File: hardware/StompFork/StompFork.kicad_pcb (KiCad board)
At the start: 2 copper layers, 100.3 x 50.8 mm, 34 parts, among them J1 Line-Level Input, J2 Direct Output, J3 Stompbox Output 1, J4 Stompbox Output 2, J5 Power, U1 TL074

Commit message: Update PCB
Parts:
- moved D1 11.4 mm to (127.0, 116.8), turned to 180 degrees
- moved J1 9.14 mm to (185.4, 88.9)
- moved J3 8.03 mm to (185.4, 109.2)
- moved J4 8.03 mm to (185.4, 99.0)
- moved R13 8.03 mm to (127.0, 114.3), turned to 180 degrees
- moved J2 7.62 mm to (185.4, 119.3)
- moved C5 7.13 mm to (175.3, 121.8), turned to 90 degrees
- moved R5 5.68 mm to (157.5, 121.9)
- moved R8 5.68 mm to (157.5, 116.8)
- moved C6 5.08 mm to (175.3, 109.1)
- moved C7 5.08 mm to (175.3, 91.5)
- moved RV2 2.62 mm to (109.2, 84.0)
- moved RV1 2.62 mm to (109.2, 96.6)
- moved R10 2.54 mm to (157.5, 101.6)
- moved R6 2.54 mm to (157.5, 111.8)
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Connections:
- J1 pad 1: Net-(J1-T) -> GND
- J1 pad 2: GND -> Net-(J1-T)
- J2 pad 1: Net-(J2-T) -> GND
- J2 pad 2: GND -> Net-(J2-T)
- J3 pad 1: Net-(J3-T) -> GND
- J3 pad 2: GND -> Net-(J3-T)
- J4 pad 1: Net-(J4-T) -> GND
- J4 pad 2: GND -> Net-(J4-T)
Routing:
- net GND: track 266.9 -> 239.0 mm
- net Net-(D2-A): track 15.9 -> 8.67 mm
- net Net-(J1-T): track 33.4 -> 26.8 mm
- net Net-(J2-T): track 24.0 -> 17.8 mm
- net Net-(J3-T): track 24.9 -> 19.9 mm
- net Net-(J4-T): track 25.0 -> 19.9 mm
- net Net-(R2-Pad1): track 96.4 -> 93.7 mm
- net Net-(U1C-+): track 55.1 -> 57.7 mm
- net Net-(R4-Pad1): track 10.2 -> 7.62 mm
- net Net-(R3-Pad1): track 10.2 -> 7.62 mm
- net Net-(C6-Pad1): track 11.2 -> 8.75 mm
- net Net-(C5-Pad1): track 10.2 -> 7.77 mm
- net Net-(C7-Pad1): track 12.3 -> 11.2 mm
- net Net-(U1D-+): track 52.5 -> 51.4 mm
- net VCC: track 35.1 -> 34.1 mm

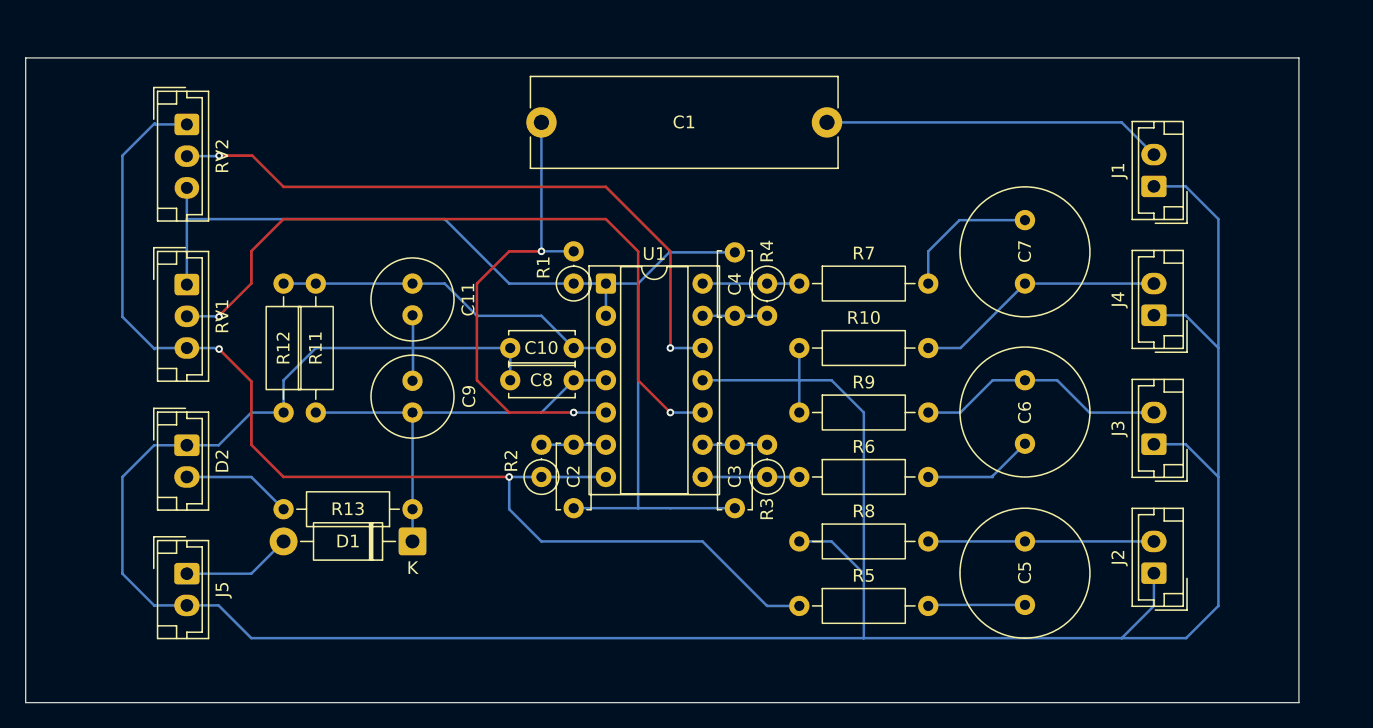
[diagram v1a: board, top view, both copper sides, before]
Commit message: Fix cap footprints
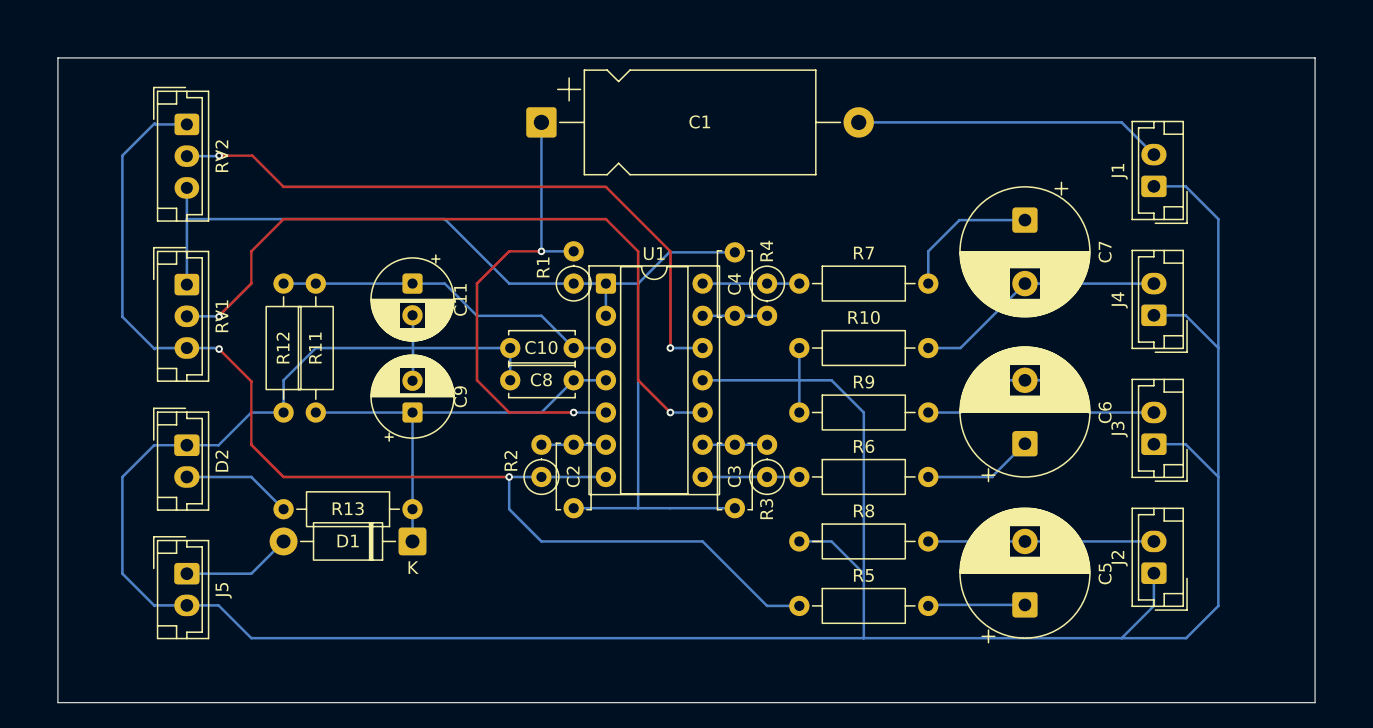
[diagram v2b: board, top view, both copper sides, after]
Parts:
- C1: footprint Capacitor_THT:C_Rect_L24.0mm_W7.0mm_P22.50mm_MKT -> Capacitor_THT:CP_Axial_L18.0mm_D8.0mm_P25.00mm_Horizontal
- C11, C9: footprint Capacitor_THT:C_Radial_D6.3mm_H11.0mm_P2.50mm -> Capacitor_THT:CP_Radial_D6.3mm_P2.50mm
- C5, C6, C7: footprint Capacitor_THT:C_Radial_D10.0mm_H12.5mm_P5.00mm -> Capacitor_THT:CP_Radial_D10.0mm_P5.00mm
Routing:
- net Net-(J1-T): track 26.8 -> 24.3 mm
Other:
- board size 100.3 x 50.8 mm -> 99.1 x 50.8 mm

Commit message: Update PCB
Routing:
- net GND: track 239.0 -> 231.4 mm
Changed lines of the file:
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@@
 	)
 	(segment
-		(start 116.84 116.84)
-		(end 114.3 119.38)
+		(start 114.3 116.84)
+		(end 116.84 116.84)
 		(width 0.2)
 		(layer "B.Cu")
@@
 	)
 	(segment
-		(start 114.3 119.38)
-		(end 109.22 119.38)
+		(start 111.76 119.38)
+		(end 114.3 116.84)
 		(width 0.2)
 		(layer "B.Cu")
 		(net 2)
+	)
+	(segment
+		(start 109.22 119.38)
+		(end 111.76 119.38)
+		(width 0.2)
+		(layer "B.Cu")
+		(net 2)
+	)
+	(segment
+		(start 147.32 114.22)
+		(end 152.4 114.22)
+		(width 0.2)
+		(layer "B.Cu")
+		(net 3)
+	)
+	(segment
+		(start 134.62 96.52)
+		(end 129.54 91.44)
+		(width 0.2)
+		(layer "B.Cu")
+		(net 3)
+	)
+	(segment
+		(start 139.7 114.22)
+		(end 144.78 114.22)
+		(width 0.2)
+		(layer "B.Cu")
+		(net 3)
+	)
+	(segment
+		(start 147.24 94.06)
+		(end 144.78 96.52)
+		(width 0.2)
+		(layer "B.Cu")
+		(net 3)
 	)
 	(segment
 		(start 129.54 91.44)
 		(end 109.22 91.44)
-		(width 0.2)
-		(layer "B.Cu")
-		(net 3)
-	)
-	(segment
-		(start 147.32 114.22)
-		(end 152.4 114.22)
-		(width 0.2)
-		(layer "B.Cu")
-		(net 3)
-	)
-	(segment
-		(start 134.62 96.52)
-		(end 129.54 91.44)
-		(width 0.2)
-		(layer "B.Cu")
-		(net 3)
-	)
-	(segment
-		(start 139.7 114.22)
-		(end 144.78 114.22)
-		(width 0.2)
-		(layer "B.Cu")
-		(net 3)
-	)
-	(segment
-		(start 147.24 94.06)
-		(end 144.78 96.52)
 		(width 0.2)
 		(layer "B.Cu")
@@
 	)
 	(segment
-		(start 111.72 109.26)
-		(end 109.22 109.26)
-		(width 0.2)
-		(layer "B.Cu")
-		(net 5)
-	)
-	(segment
 		(start 185.42 88.86)
 		(end 187.92 88.86)
@@
 	)
 	(segment
+		(start 190.5 116.84)
+		(end 190.5 111.76)
+		(width 0.2)
+		(layer "B.Cu")
+		(net 5)
+	)
+	(segment
 		(start 162.56 119.38)
 		(end 162.56 124.46)
@@
 	)
 	(segment
-		(start 114.3 106.68)
-		(end 111.72 109.26)
-		(width 0.2)
-		(layer "B.Cu")
-		(net 5)
-	)
-	(segment
-		(start 162.56 124.46)
-		(end 114.3 124.46)
-		(width 0.2)
-		(layer "B.Cu")
-		(net 5)
-	)
-	(segment
-		(start 190.5 111.76)
-		(end 190.5 121.92)
-		(width 0.2)
-		(layer "B.Cu")
-		(net 5)
-	)
-	(segment
 		(start 160.02 104.14)
 		(end 162.56 106.68)
@@
 	)
 	(segment
-		(start 190.5 121.92)
-		(end 187.96 124.46)
+		(start 149.86 121.92)
+		(end 152.4 124.46)
 		(width 0.2)
 		(layer "B.Cu")
@@
 	)
 	(segment
-		(start 114.3 124.46)
-		(end 111.72 121.88)
-		(width 0.2)
-		(layer "B.Cu")
-		(net 5)
-	)
-	(segment
-		(start 116.84 106.68)
-		(end 114.3 106.68)
+		(start 185.42 119.34)
+		(end 187.92 119.34)
+		(width 0.2)
+		(layer "B.Cu")
+		(net 5)
+	)
+	(segment
+		(start 152.4 124.46)
+		(end 162.56 124.46)
 		(width 0.2)
 		(layer "B.Cu")
@@
 	)
 	(segment
+		(start 111.76 121.92)
+		(end 149.86 121.92)
+		(width 0.2)
+		(layer "B.Cu")
+		(net 5)
+	)
+	(segment
 		(start 104.14 119.38)
 		(end 104.14 111.76)
@@
 	)
 	(segment
-		(start 111.72 121.88)
-		(end 109.22 121.88)
-		(width 0.2)
-		(layer "B.Cu")
-		(net 5)
-	)
-	(segment
-		(start 187.96 124.46)
-		(end 182.88 124.46)
-		(width 0.2)
-		(layer "B.Cu")
-		(net 5)
-	)
-	(segment
 		(start 149.86 104.14)
 		(end 160.02 104.14)
@@
 	)
 	(segment
+		(start 111.72 109.26)
+		(end 114.3 106.68)
+		(width 0.2)
+		(layer "B.Cu")
+		(net 5)
+	)
+	(segment
 		(start 106.72 121.88)
 		(end 106.68 121.92)
@@
 	)
 	(segment
+		(start 109.22 109.26)
+		(end 111.72 109.26)
+		(width 0.2)
+		(layer "B.Cu")
+		(net 5)
+	)
+	(segment
 		(start 134.7 104.14)
 		(end 134.7 101.6)
@@
 	)
 	(segment
+		(start 109.22 121.88)
+		(end 111.72 121.88)
+		(width 0.2)
+		(layer "B.Cu")
+		(net 5)
+	)
+	(segment
 		(start 162.56 106.68)
 		(end 162.56 114.3)
@@
 	)
 	(segment
+		(start 111.72 121.88)
+		(end 111.76 121.92)
+		(width 0.2)
+		(layer "B.Cu")
+		(net 5)
+	)
+	(segment
 		(start 187.92 109.18)
 		(end 190.5 111.76)
@@
 	)
 	(segment
-		(start 114.38 86.44)
-		(end 111.76 86.44)
+		(start 187.92 119.34)
+		(end 187.96 119.38)
+		(width 0.2)
+		(layer "B.Cu")
+		(net 5)
+	)
+	(segment
+		(start 187.96 119.38)
+		(end 190.5 116.84)
+		(width 0.2)
+		(layer "B.Cu")
+		(net 5)
+	)
+	(segment
+		(start 114.3 106.68)
+		(end 116.84 106.68)
+		(width 0.2)
+		(layer "B.Cu")
+		(net 5)
+	)
+	(segment
+		(start 111.76 86.44)
+		(end 114.38 86.44)
 		(width 0.2)
 		(layer "F.Cu")
@@
 	)
 	(segment
+		(start 111.76 99.14)
+		(end 111.76 99.06)
+		(width 0.2)
+		(layer "F.Cu")
+		(net 10)
+	)
+	(segment
+		(start 111.76 99.06)
+		(end 114.3 96.52)
+		(width 0.2)
+		(layer "F.Cu")
+		(net 10)
+	)
+	(segment
 		(start 116.84 91.44)
 		(end 142.24 91.44)
@@
 		(start 114.3 93.98)
 		(end 116.84 91.44)
-		(width 0.2)
-		(layer "F.Cu")
-		(net 10)
-	)
-	(segment
-		(start 111.76 99.06)
-		(end 114.3 96.52)
-		(width 0.2)
-		(layer "F.Cu")
-		(net 10)
-	)
-	(segment
-		(start 111.76 99.14)
-		(end 111.76 99.06)
 		(width 0.2)
 		(layer "F.Cu")
@@
 	)
 	(segment
+		(start 111.76 101.68)
+		(end 111.84 101.68)
+		(width 0.2)
+		(layer "F.Cu")
+		(net 19)
+	)
+	(segment
 		(start 114.3 109.22)
 		(end 116.84 111.76)
@@
 	)
 	(segment
-		(start 111.76 101.68)
-		(end 114.3 104.22)
+		(start 111.84 101.68)
+		(end 114.3 104.14)
 		(width 0.2)
 		(layer "F.Cu")
@@
 	)
 	(segment
-		(start 116.84 114.3)
-		(end 114.3 111.76)
+		(start 109.22 111.76)
+		(end 111.76 111.76)
 		(width 0.2)
 		(layer "B.Cu")
@@
 	)
 	(segment
-		(start 114.3 111.76)
-		(end 109.22 111.76)
-		(width 0.2)
-		(layer "B.Cu")
+		(start 111.76 111.76)
+		(end 114.3 114.3)
+		(width 0.2)
+		(layer "B.Cu")
+		(net 22)
+	)
+	(segment
+		(start 114.3 114.3)
+		(end 116.84 114.3)
+		(width 0.2)
+		(layer "B.Cu")
